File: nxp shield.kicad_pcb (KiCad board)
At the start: 2 copper layers, 91.4 x 54.6 mm, 10 parts, among them J1 Conn_02x10_Counter_Clockwise, J2 Conn_02x08_Top_Bottom, J3 Conn_02x08_Top_Bottom, J4 Conn_02x06_Top_Bottom, J5 Conn_01x08, J6 Conn_01x08

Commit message: fixed spacing
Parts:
- removed J1: Conn_02x10_Counter_Clockwise, Connector_PinHeader_2.54mm:PinHeader_2x10_P2.54mm_Vertical
- removed J2, J3: Conn_02x08_Top_Bottom, Connector_PinHeader_2.54mm:PinHeader_2x08_P2.54mm_Vertical
- removed J4: Conn_02x06_Top_Bottom, Connector_PinHeader_2.54mm:PinHeader_2x06_P2.54mm_Vertical
- removed J5, J6: Conn_01x08, Connector_PinHeader_2.54mm:PinHeader_1x08_P2.54mm_Vertical
- added U1: ~, frdm-mcxa153:FRDM-MCXA153, F.Cu at (139.6, 121.6)
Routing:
- net unconnected-(J7-Pin_3-Pad3): track 0.91 -> 0.00 mm
- net 3v3: track 0.00 -> 0.91 mm
- net unconnected-(U1-P2_7-Pad63): track 0.00 -> 0.71 mm
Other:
- board text removed: "help me"

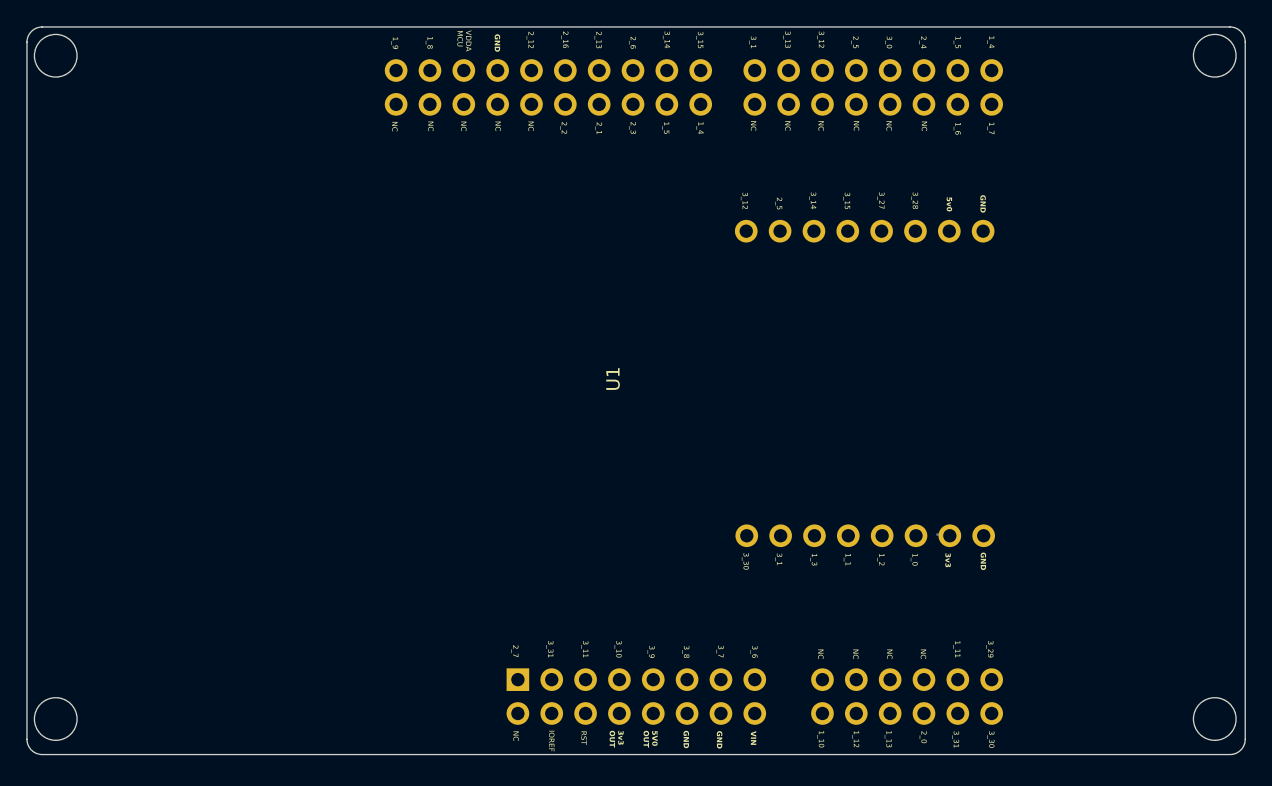
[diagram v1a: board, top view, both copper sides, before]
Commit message: fixed footprint, pin numbering and added ground plane
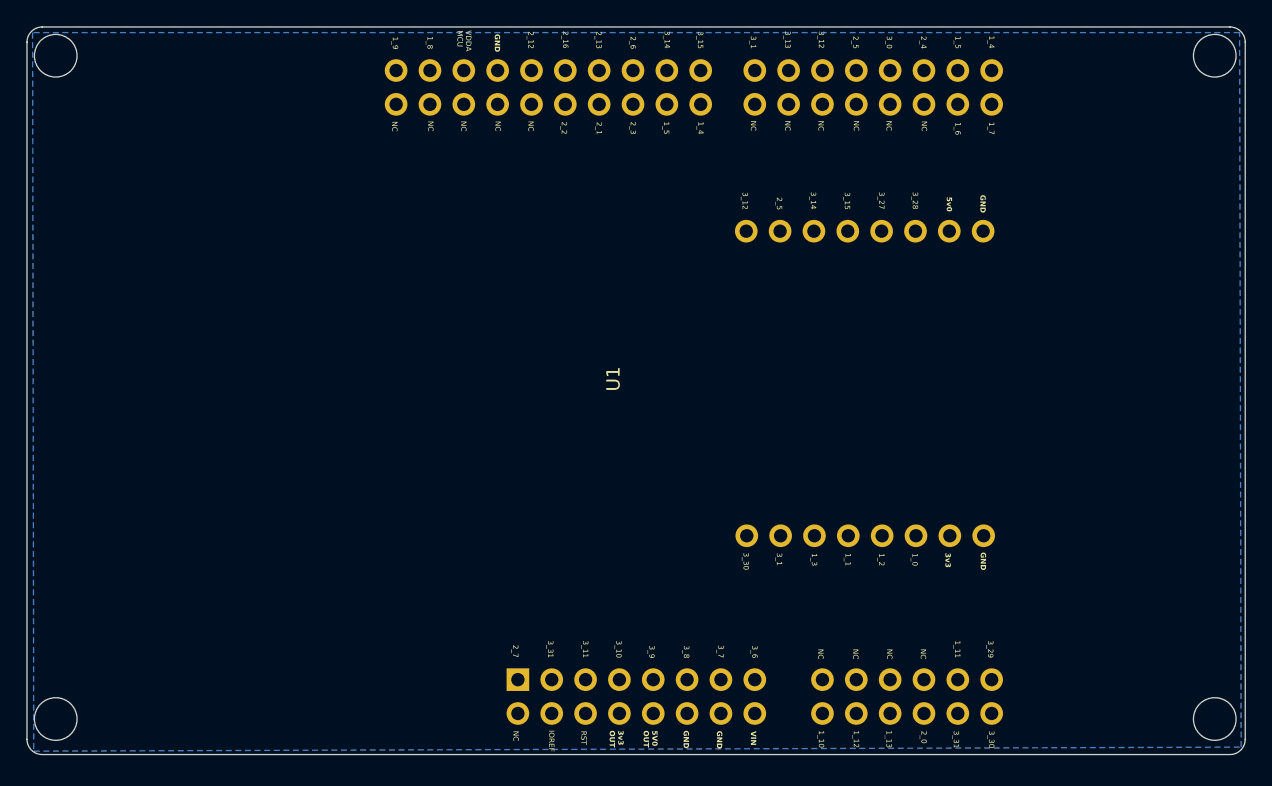
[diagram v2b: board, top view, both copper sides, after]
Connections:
- net 3v3 renamed +3.3V
- net SCA renamed SCl
- U1 pad 67: unconnected-(U1-5V0-Pad67) -> +5V
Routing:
- net +3.3V: track 0.91 -> 0.00 mm
- added copper zone on B.Cu, net GND
